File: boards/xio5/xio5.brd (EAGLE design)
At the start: 170 x 170 mm, 92 parts, among them IC1 TC74LCX138FT, IC2 XRA1405IL24-F, J1 98424-G52-14ALF

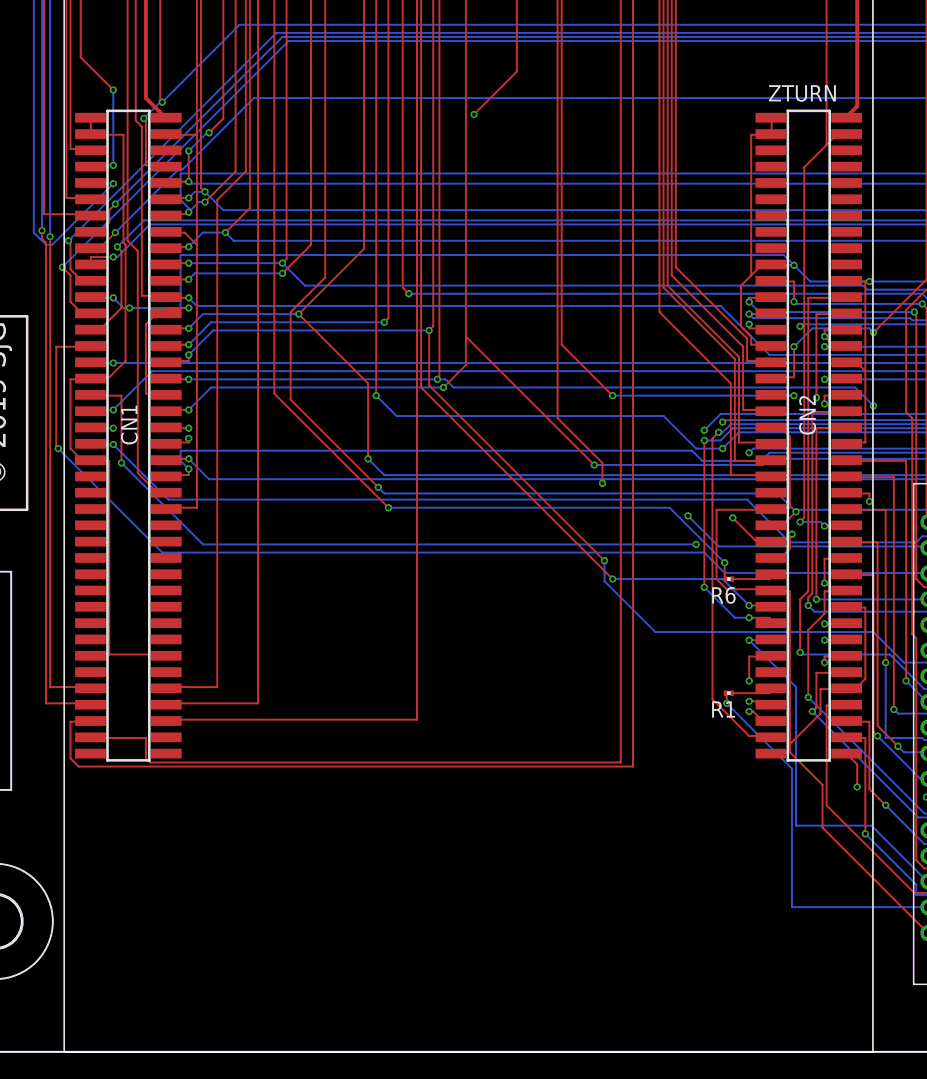
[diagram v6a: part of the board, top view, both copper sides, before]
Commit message: Board parts verified. Circuit to be checked. BOM manipulated a bit, save $500 @ q50, or $140 @ q5
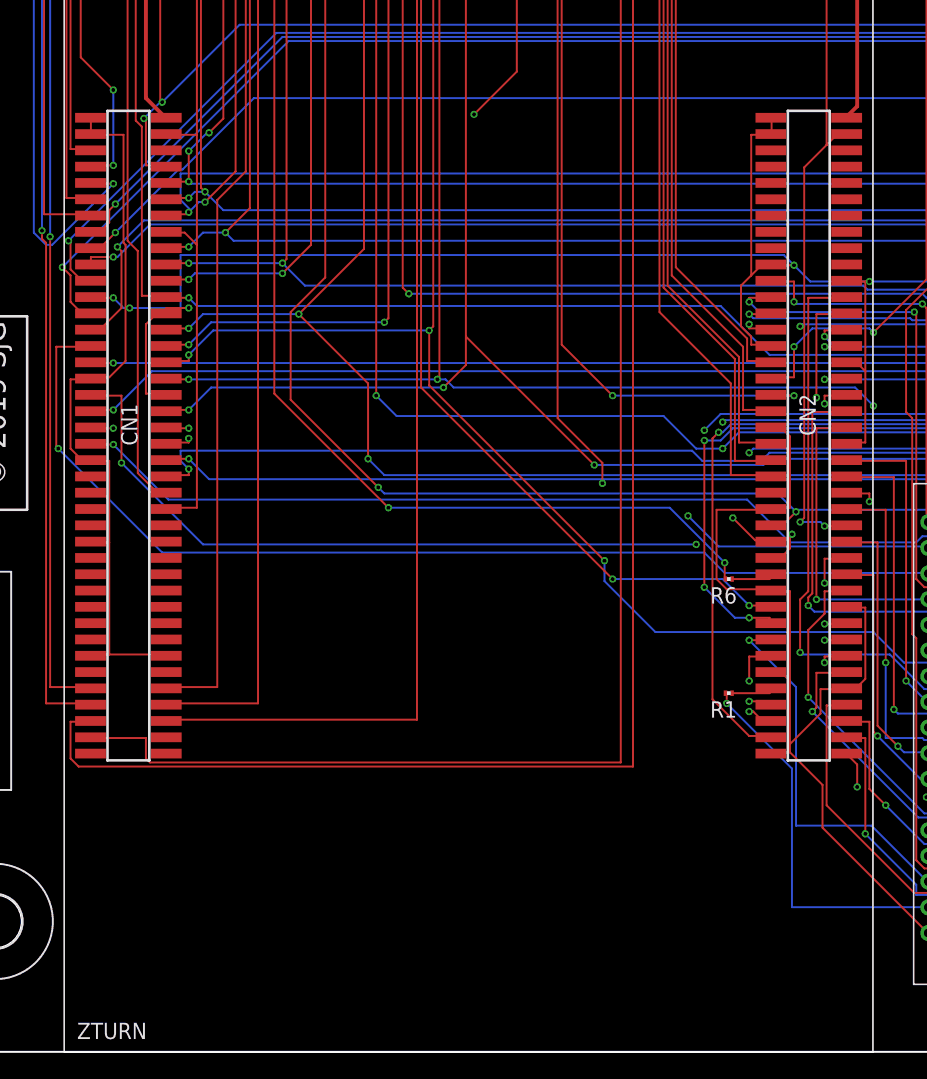
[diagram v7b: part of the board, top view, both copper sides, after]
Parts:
- IC1: value TC74LCX138FT -> SN74LVC138APWR
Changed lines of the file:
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@@
 <attribute name="VALUE" x="135.458" y="87.1885" size="0.4064" layer="27" ratio="10" rot="R180"/>
 </element>
-<element name="H3" library="holes" library_urn="urn:adsk.eagle:library:237" package="4,1" package3d_urn="urn:adsk.eagle:package:14273/1" value="MOUNT-HOLE4.1" x="6.35" y="10.16" smashed="yes"/>
-<element name="H6" library="holes" library_urn="urn:adsk.eagle:library:237" package="4,1" package3d_urn="urn:adsk.eagle:package:14273/1" value="MOUNT-HOLE4.1" x="6.35" y="165.1" smashed="yes"/>
-<element name="H7" library="holes" library_urn="urn:adsk.eagle:library:237" package="4,1" package3d_urn="urn:adsk.eagle:package:14273/1" value="MOUNT-HOLE4.1" x="163.83" y="165.1" smashed="yes"/>
-<element name="H8" library="holes" library_urn="urn:adsk.eagle:library:237" package="4,1" package3d_urn="urn:adsk.eagle:package:14273/1" value="MOUNT-HOLE4.1" x="163.83" y="33.02" smashed="yes"/>
+<element name="H3" library="holes" library_urn="urn:adsk.eagle:library:237" package="4,1" package3d_urn="urn:adsk.eagle:package:14273/1" value="MOUNT-HOLE4.1" x="6.35" y="10.16" smashed="yes">
+<attribute name="NOSTUFF" value="1" x="6.35" y="10.16" size="1.778" layer="27" display="off"/>
+</element>
+<element name="H6" library="holes" library_urn="urn:adsk.eagle:library:237" package="4,1" package3d_urn="urn:adsk.eagle:package:14273/1" value="MOUNT-HOLE4.1" x="6.35" y="165.1" smashed="yes">
+<attribute name="NOSTUFF" value="1" x="6.35" y="165.1" size="1.778" layer="27" display="off"/>
+</element>
+<element name="H7" library="holes" library_urn="urn:adsk.eagle:library:237" package="4,1" package3d_urn="urn:adsk.eagle:package:14273/1" value="MOUNT-HOLE4.1" x="163.83" y="165.1" smashed="yes">
+<attribute name="NOSTUFF" value="1" x="163.83" y="165.1" size="1.778" layer="27" display="off"/>
+</element>
+<element name="H8" library="holes" library_urn="urn:adsk.eagle:library:237" package="4,1" package3d_urn="urn:adsk.eagle:package:14273/1" value="MOUNT-HOLE4.1" x="163.83" y="33.02" smashed="yes">
+<attribute name="NOSTUFF" value="1" x="163.83" y="33.02" size="1.778" layer="27" display="off"/>
+</element>
 <element name="U$3" library="sjg-con" package="MINI-SAS" value="MINI-SAS" x="157.48" y="78.64" smashed="yes" rot="R90">
 <attribute name="NAME" x="152.68" y="69.84" size="0.6096" layer="21" rot="R180"/>
@@
 </element>
 <element name="ZTURN" library="pbxl" package="ZTURN" value="ZTURN" x="43.73" y="48" smashed="yes">
-<attribute name="NAME" x="12.73" y="1" size="1.27" layer="21"/>
 <attribute name="NAME" x="13.555" y="74.035" size="1.27" layer="25"/>
 <attribute name="NAME" x="66.555" y="74.035" size="1.27" layer="25"/>
+<attribute name="NAME" x="12.73" y="1" size="1.27" layer="21"/>
+<attribute name="NOSTUFF" value="1" x="43.73" y="48" size="1.778" layer="27" display="off"/>
 <attribute name="VALUE" x="71.035" y="44.19" size="1.27" layer="27" rot="R90"/>
 </element>
@@
 <attribute name="RS_PART_NUMBER" value="1822960" x="7.27" y="117.13" size="1.778" layer="27" rot="R270" display="off"/>
 <attribute name="RS_PRICE-STOCK" value="http://uk.rs-online.com/web/p/products/1822960" x="7.27" y="117.13" size="1.778" layer="27" rot="R270" display="off"/>
+<attribute name="USE" value="98424-G52-14ALF" x="7.27" y="117.13" size="1.778" layer="27" rot="R270" display="off"/>
 <attribute name="VALUE" x="7.27" y="117.13" size="1.27" layer="27" rot="R270" align="center"/>
 </element>
 <element name="JP1" library="pinhead" library_urn="urn:adsk.eagle:library:325" package="1X07" package3d_urn="urn:adsk.eagle:package:22477/2" value="" x="3" y="140.4" smashed="yes" rot="R270">
 <attribute name="NAME" x="1.0338" y="129.2288" size="1.27" layer="25" ratio="10"/>
+<attribute name="NOSTUFF" value="1" x="3" y="140.4" size="1.778" layer="27" rot="R270" display="off"/>
 <attribute name="POPULARITY" value="0" x="3" y="140.4" size="1.778" layer="27" rot="R270" display="off"/>
 <attribute name="VALUE" x="-0.175" y="149.29" size="1.27" layer="27" rot="R270"/>
 </element>
-<element name="IC1" library="samacsys" package="SOP65P640X120-16N" value="TC74LCX138FT" x="91.44" y="58.42" smashed="yes" rot="R90">
+<element name="IC1" library="samacsys" package="SOP65P640X120-16N" value="SN74LVC138APWR" x="91.44" y="58.42" smashed="yes" rot="R90">
 <attribute name="DESCRIPTION" value="Toshiba TC74LCX138FT, Decoder, Demultiplexer, 1-of-8, Inverting, 1.65  3.6 V, 16-Pin TSSOP" x="91.44" y="58.42" size="1.778" layer="27" rot="R90" display="off"/>
 <attribute name="HEIGHT" value="1.2mm" x="91.44" y="58.42" size="1.778" layer="27" rot="R90" display="off"/>
@@
 <attribute name="RS_PART_NUMBER" value="4063409" x="91.44" y="58.42" size="1.778" layer="27" rot="R90" display="off"/>
 <attribute name="RS_PRICE-STOCK" value="http://uk.rs-online.com/web/p/products/4063409" x="91.44" y="58.42" size="1.778" layer="27" rot="R90" display="off"/>
+<attribute name="USE" value="SN74LVC138APWR" x="91.44" y="58.42" size="1.778" layer="27" rot="R90" display="off"/>
 <attribute name="VALUE" x="91.44" y="58.42" size="1.27" layer="27" rot="R90" align="center"/>
 </element>
@@
 <attribute name="RS_PART_NUMBER" value="" x="102.87" y="58.42" size="1.778" layer="27" rot="R180" display="off"/>
 <attribute name="RS_PRICE-STOCK" value="" x="102.87" y="58.42" size="1.778" layer="27" rot="R180" display="off"/>
+<attribute name="USE" value="XRA1405IL24-F" x="102.87" y="58.42" size="1.778" layer="27" rot="R180" display="off"/>
 <attribute name="VALUE" x="102.87" y="58.42" size="1.27" layer="27" rot="R180" align="center"/>
 </element>
@@
 <element name="JP2" library="pinhead-2" package="2X20M" value="" x="38.1" y="107.95" smashed="yes">
 <attribute name="NAME" x="17.1" y="105.95" size="1.016" layer="25" ratio="14" rot="R90"/>
+<attribute name="USE" value="SBH21-NBPN-D20-ST-BK" x="38.1" y="107.95" size="1.778" layer="27" display="off"/>
 <attribute name="VALUE" x="60.1" y="105.95" size="0.8128" layer="27" ratio="10" rot="R90"/>
 </element>
@@
 <element name="JP4" library="pinhead-2" package="2X04M" value="" x="83.82" y="144.78" smashed="yes">
 <attribute name="NAME" x="78.82" y="142.78" size="1.016" layer="25" ratio="14" rot="R90"/>
+<attribute name="NOSTUFF" value="1" x="83.82" y="144.78" size="1.778" layer="27" display="off"/>
 <attribute name="VALUE" x="89.82" y="142.78" size="0.8128" layer="27" ratio="10" rot="R90"/>
 </element>
 <element name="JP5" library="pinhead-2" package="2X04M" value="" x="110.49" y="144.78" smashed="yes">
 <attribute name="NAME" x="105.49" y="142.78" size="1.016" layer="25" ratio="14" rot="R90"/>
+<attribute name="NOSTUFF" value="1" x="110.49" y="144.78" size="1.778" layer="27" display="off"/>
 <attribute name="VALUE" x="116.49" y="142.78" size="0.8128" layer="27" ratio="10" rot="R90"/>
 </element>

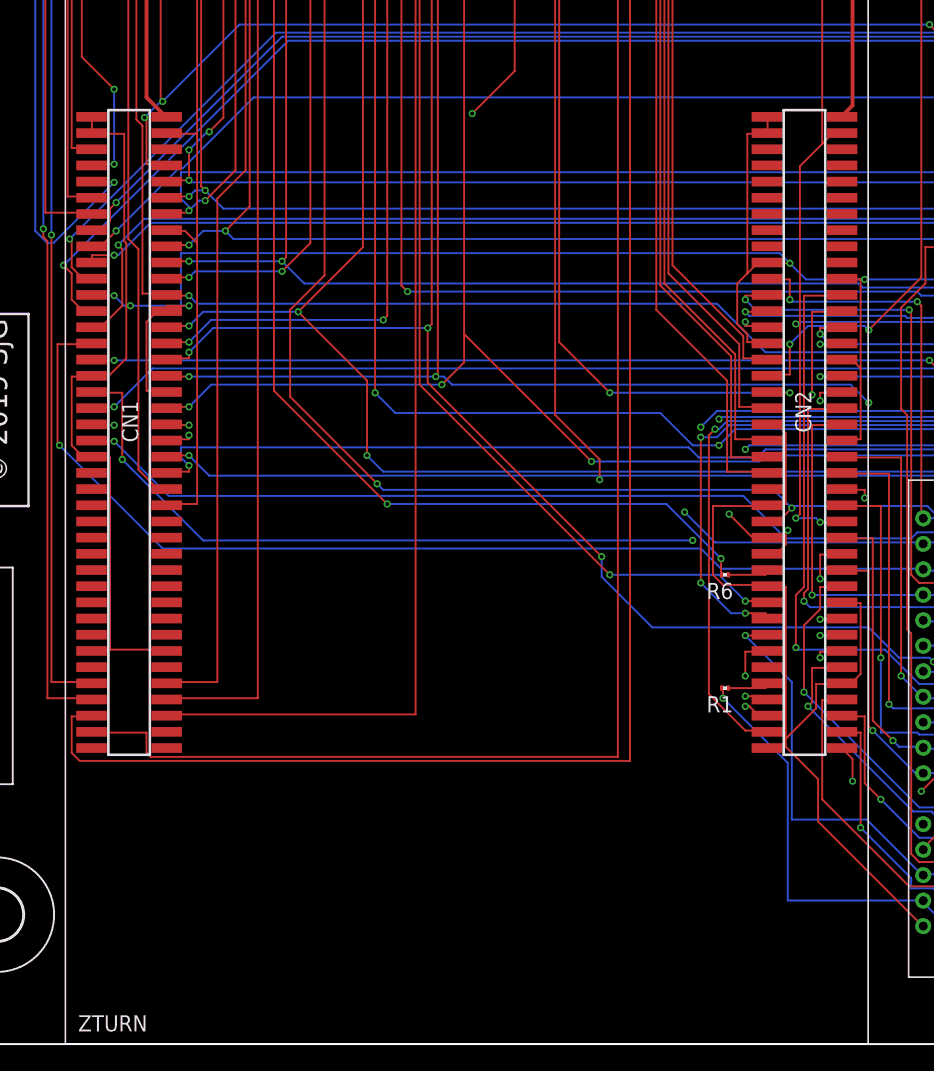
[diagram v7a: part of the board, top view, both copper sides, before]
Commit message: Add two connectors to stand in for the Zynq board
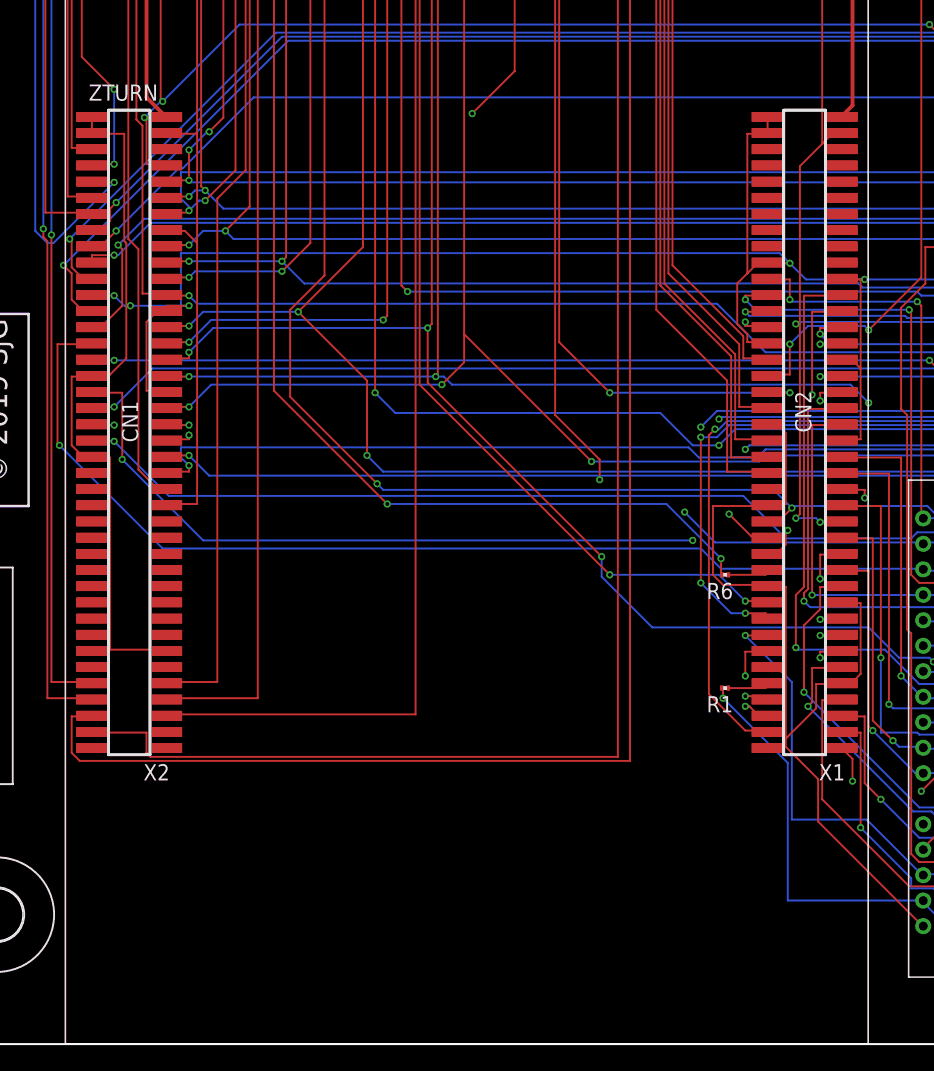
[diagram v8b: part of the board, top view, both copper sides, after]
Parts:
- added X1, X2: 1365-80, con-leotronics:1365-80
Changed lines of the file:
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@@
 <drawing>
 <settings>
-<setting alwaysvectorfont="yes"/>
+<setting alwaysvectorfont="no"/>
 <setting verticaltext="up"/>
 </settings>
-<grid distance="0.05" unitdist="inch" unit="inch" style="lines" multiple="1" display="yes" altdistance="1" altunitdist="mil" altunit="mil"/>
+<grid distance="1" unitdist="mm" unit="mm" style="lines" multiple="1" display="yes" altdistance="1" altunitdist="mil" altunit="mil"/>
 <layers>
 <layer number="1" name="Top" color="4" fill="1" visible="yes" active="yes"/>
@@
 </element>
 <element name="ZTURN" library="pbxl" package="ZTURN" value="ZTURN" x="43.73" y="48" smashed="yes">
-<attribute name="NAME" x="13.555" y="74.035" size="1.27" layer="25"/>
 <attribute name="NAME" x="66.555" y="74.035" size="1.27" layer="25"/>
 <attribute name="NAME" x="12.73" y="1" size="1.27" layer="21"/>
+<attribute name="NAME" x="13.555" y="74.035" size="1.27" layer="25"/>
 <attribute name="NOSTUFF" value="1" x="43.73" y="48" size="1.778" layer="27" display="off"/>
 <attribute name="VALUE" x="71.035" y="44.19" size="1.27" layer="27" rot="R90"/>
@@
 <attribute name="VALUE" x="120.015" y="127" size="1.27" layer="27" rot="R90"/>
 </element>
+<element name="X1" library="con-leotronics" library_urn="urn:adsk.eagle:library:160" package="1365-80" package3d_urn="urn:adsk.eagle:package:7997/1" value="1365-80" x="69.75" y="48" smashed="yes" rot="R90">
+<attribute name="MF" value="" x="69.75" y="48" size="1.778" layer="27" rot="R90" display="off"/>
+<attribute name="MPN" value="" x="69.75" y="48" size="1.778" layer="27" rot="R90" display="off"/>
+<attribute name="NAME" x="72.925" y="21.965" size="1.27" layer="25" rot="R180"/>
+<attribute name="OC_FARNELL" value="unknown" x="69.75" y="48" size="1.778" layer="27" rot="R90" display="off"/>
+<attribute name="OC_NEWARK" value="unknown" x="69.75" y="48" size="1.778" layer="27" rot="R90" display="off"/>
+<attribute name="POPULARITY" value="0" x="69.75" y="48" size="1.778" layer="27" rot="R90" display="off"/>
+<attribute name="VALUE" x="73.56" y="75.305" size="1.27" layer="27" rot="R180"/>
+</element>
+<element name="X2" library="con-leotronics" library_urn="urn:adsk.eagle:library:160" package="1365-80" package3d_urn="urn:adsk.eagle:package:7997/1" value="1365-80" x="16.75" y="48" smashed="yes" rot="R90">
+<attribute name="MF" value="" x="16.75" y="48" size="1.778" layer="27" rot="R90" display="off"/>
+<attribute name="MPN" value="" x="16.75" y="48" size="1.778" layer="27" rot="R90" display="off"/>
+<attribute name="NAME" x="19.925" y="21.965" size="1.27" layer="25" rot="R180"/>
+<attribute name="OC_FARNELL" value="unknown" x="16.75" y="48" size="1.778" layer="27" rot="R90" display="off"/>
+<attribute name="OC_NEWARK" value="unknown" x="16.75" y="48" size="1.778" layer="27" rot="R90" display="off"/>
+<attribute name="POPULARITY" value="0" x="16.75" y="48" size="1.778" layer="27" rot="R90" display="off"/>
+<attribute name="VALUE" x="20.56" y="75.305" size="1.27" layer="27" rot="R180"/>
+</element>
 </elements>
